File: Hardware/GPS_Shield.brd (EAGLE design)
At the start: 59.7 x 53.3 mm, 52 parts, among them J1 ARDUINO_R3_SHIELD, J2 USD_CONNECTOR, J3 DNP (GP-735-VERTICAL), U1 APK2112-3.3V, U2 GP3906-TLP, U3 TXB0108

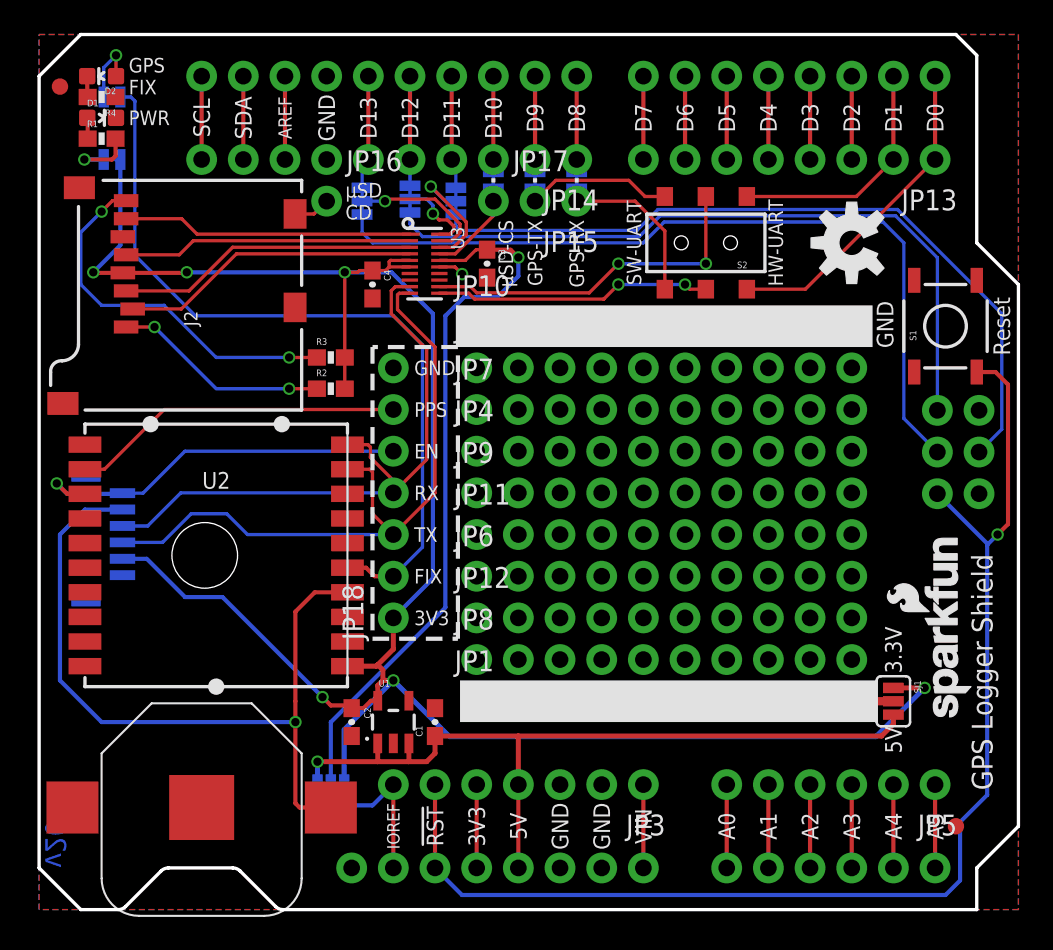
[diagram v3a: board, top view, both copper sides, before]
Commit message: Upping isolate to 0.01", adding some GND vias.
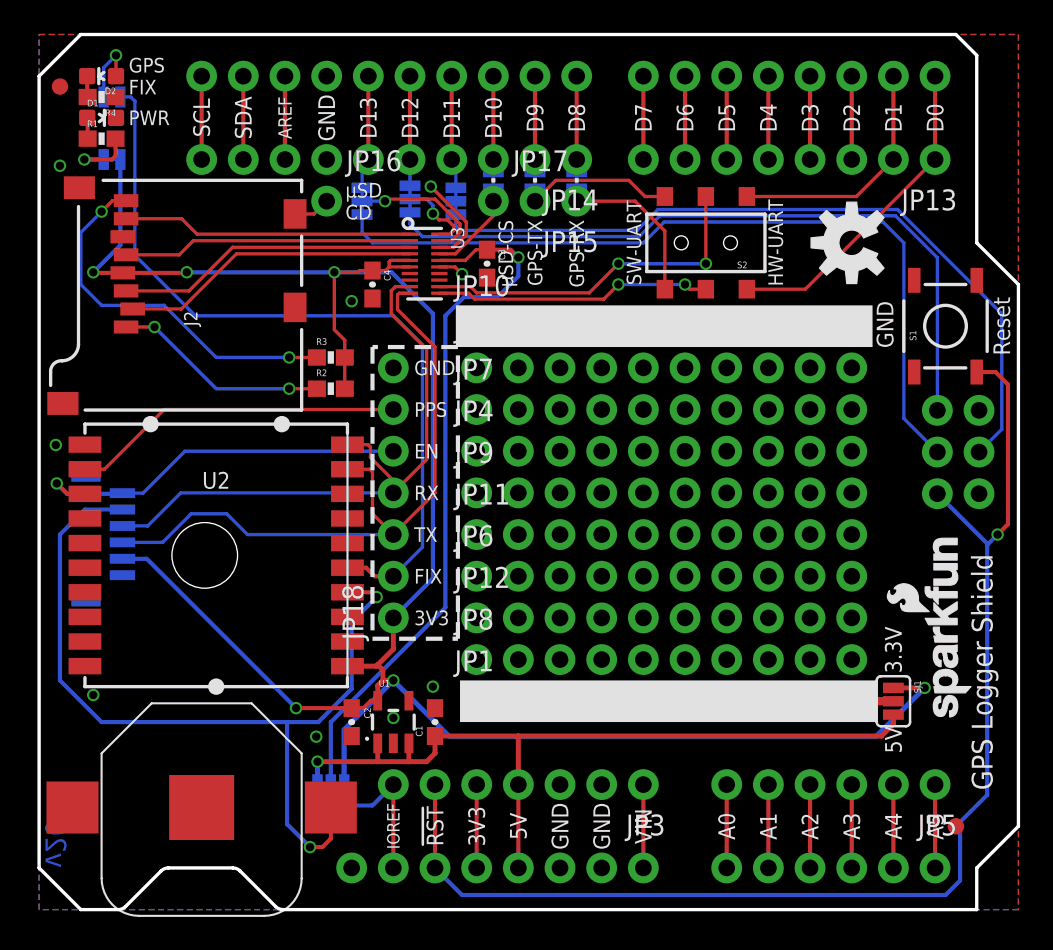
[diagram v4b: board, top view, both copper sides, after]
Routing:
- net V_BATT: track 46.3 -> 52.7 mm, vias 1 -> 2
- net 3.3V: track 134.0 -> 135.1 mm
- net GND: vias 1 -> 8
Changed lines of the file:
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@@
 <layer number="47" name="Measures" color="7" fill="1" visible="no" active="yes"/>
 <layer number="48" name="Document" color="7" fill="1" visible="no" active="yes"/>
-<layer number="49" name="Reference" color="7" fill="1" visible="yes" active="yes"/>
+<layer number="49" name="Reference" color="7" fill="1" visible="no" active="yes"/>
 <layer number="50" name="dxf" color="7" fill="1" visible="no" active="yes"/>
 <layer number="51" name="tDocu" color="6" fill="1" visible="yes" active="yes"/>
@@
 <contactref element="C4" pad="2"/>
 <contactref element="D1" pad="C"/>
-<polygon width="0.3048" layer="1" isolate="0.1524">
+<polygon width="0.254" layer="1" isolate="0.254">
 <vertex x="0" y="53.34"/>
 <vertex x="59.69" y="53.34"/>
@@
 <vertex x="0" y="0"/>
 </polygon>
-<polygon width="0.3048" layer="16" isolate="0.1524">
+<polygon width="0.254" layer="16" isolate="0.254">
 <vertex x="0" y="53.34"/>
 <vertex x="59.69" y="53.34"/>
@@
 <contactref element="J2" pad="GND3"/>
 <contactref element="J2" pad="GND"/>
+<via x="19.05" y="37.084" extent="1-16" drill="0.508"/>
+<via x="21.59" y="11.684" extent="1-16" drill="0.508"/>
+<via x="16.891" y="10.541" extent="1-16" drill="0.508"/>
+<via x="24.003" y="13.589" extent="1-16" drill="0.508"/>
+<via x="3.302" y="13.081" extent="1-16" drill="0.508"/>
+<via x="1.016" y="28.321" extent="1-16" drill="0.508"/>
+<via x="1.27" y="45.339" extent="1-16" drill="0.508"/>
 </signal>
 <signal name="3.3V">
@@
 <wire x1="22.595" y1="39.17" x2="21.336" y2="39.17" width="0.2032" layer="1"/>
 <via x="9.001575" y="38.846575" extent="1-16" drill="0.508"/>
-<wire x1="9.001575" y1="38.846575" x2="18.63" y2="38.846575" width="0.254" layer="16"/>
-<via x="18.63" y="38.846575" extent="1-16" drill="0.508"/>
+<wire x1="9.001575" y1="38.846575" x2="17.995" y2="38.846575" width="0.254" layer="16"/>
+<via x="17.995" y="38.846575" extent="1-16" drill="0.508"/>
 <wire x1="24.003" y1="36.322" x2="24.003" y2="20.193" width="0.254" layer="16"/>
 <wire x1="20.64" y1="12.7301" x2="20.2231" y2="12.7301" width="0.254" layer="1"/>
 <wire x1="20.2231" y1="12.7301" x2="19.773" y2="12.28" width="0.254" layer="1"/>
-<wire x1="19.05" y1="12.28" x2="19.773" y2="12.28" width="0.254" layer="1"/>
 <contactref element="JP18" pad="1"/>
 <wire x1="24.003" y1="20.193" x2="21.59" y2="17.78" width="0.254" layer="16"/>
-<wire x1="18.63" y1="38.846575" x2="21.478425" y2="38.846575" width="0.254" layer="16"/>
+<wire x1="17.995" y1="38.846575" x2="21.478425" y2="38.846575" width="0.254" layer="16"/>
 <wire x1="21.478425" y1="38.846575" x2="24.003" y2="36.322" width="0.254" layer="16"/>
 <wire x1="22.595" y1="39.57" x2="21.409" y2="39.57" width="0.2032" layer="1"/>
@@
 <wire x1="20.32" y1="38.95" x2="19.534425" y2="38.95" width="0.2032" layer="1"/>
 <wire x1="19.534425" y1="38.95" x2="19.431" y2="38.846575" width="0.2032" layer="1"/>
-<wire x1="18.63" y1="38.846575" x2="19.431" y2="38.846575" width="0.2032" layer="1"/>
+<wire x1="17.995" y1="38.846575" x2="19.431" y2="38.846575" width="0.2032" layer="1"/>
 <wire x1="21.336" y1="39.17" x2="21.116" y2="38.95" width="0.2032" layer="1"/>
 <wire x1="21.116" y1="38.95" x2="20.32" y2="38.95" width="0.2032" layer="1"/>
@@
 <wire x1="3.338575" y1="38.81" x2="3.302" y2="38.846575" width="0.254" layer="1"/>
 <wire x1="18.63" y1="31.75" x2="18.63" y2="33.655" width="0.2032" layer="1"/>
-<wire x1="18.63" y1="38.846575" x2="18.63" y2="33.655" width="0.2032" layer="1"/>
 <contactref element="J3" pad="2"/>
 <wire x1="5.08" y1="21.3835" x2="6.5565" y2="21.3835" width="0.254" layer="16"/>
-<via x="17.273" y="12.953" extent="1-16" drill="0.508"/>
-<wire x1="17.273" y1="12.953" x2="11.176" y2="19.05" width="0.254" layer="16"/>
-<wire x1="11.176" y1="19.05" x2="8.89" y2="19.05" width="0.254" layer="16"/>
-<wire x1="8.89" y1="19.05" x2="6.5565" y2="21.3835" width="0.254" layer="16"/>
-<wire x1="18.885" y1="12.445" x2="17.781" y2="12.445" width="0.254" layer="1"/>
-<wire x1="17.781" y1="12.445" x2="17.273" y2="12.953" width="0.254" layer="1"/>
+<wire x1="18.63" y1="33.655" x2="18.63" y2="34.71" width="0.2032" layer="1"/>
+<wire x1="17.995" y1="38.846575" x2="17.995" y2="35.345" width="0.2032" layer="1"/>
+<wire x1="17.995" y1="35.345" x2="18.63" y2="34.71" width="0.2032" layer="1"/>
+<wire x1="6.5565" y1="21.3835" x2="15.66" y2="12.28" width="0.254" layer="16"/>
+<via x="15.66" y="12.28" extent="1-16" drill="0.508"/>
+<wire x1="15.66" y1="12.28" x2="19.05" y2="12.28" width="0.254" layer="1"/>
+<wire x1="19.773" y1="12.28" x2="19.05" y2="12.28" width="0.254" layer="1"/>
 </signal>
 <signal name="5V">
@@
 <contactref element="J3" pad="5"/>
 <contactref element="U2" pad="4"/>
-<wire x1="15.621" y1="6.477" x2="15.621" y2="11.43" width="0.254" layer="1"/>
-<wire x1="15.621" y1="12.7" x2="15.621" y2="18.161" width="0.254" layer="1"/>
-<wire x1="18.795" y1="19.34" x2="16.8" y2="19.34" width="0.254" layer="1"/>
-<wire x1="16.8" y1="19.34" x2="15.621" y2="18.161" width="0.254" layer="1"/>
-<wire x1="15.621" y1="6.477" x2="15.875" y2="6.223" width="0.254" layer="1"/>
-<wire x1="17.78" y1="6.223" x2="15.875" y2="6.223" width="0.254" layer="1"/>
 <wire x1="5.08" y1="24.3835" x2="2.7935" y2="24.3835" width="0.254" layer="16"/>
 <wire x1="2.7935" y1="24.3835" x2="1.27" y2="22.86" width="0.254" layer="16"/>
 <wire x1="1.27" y1="22.86" x2="1.27" y2="13.97" width="0.254" layer="16"/>
 <wire x1="1.27" y1="13.97" x2="3.81" y2="11.43" width="0.254" layer="16"/>
-<wire x1="3.81" y1="11.43" x2="15.621" y2="11.43" width="0.254" layer="16"/>
-<via x="15.621" y="11.43" extent="1-16" drill="0.508"/>
-<wire x1="15.621" y1="11.43" x2="15.621" y2="12.7" width="0.254" layer="1"/>
+<wire x1="3.81" y1="11.43" x2="15.113" y2="11.43" width="0.254" layer="16"/>
+<wire x1="15.113" y1="11.43" x2="17.018" y2="11.43" width="0.254" layer="16"/>
+<wire x1="18.795" y1="19.34" x2="20.284" y2="19.34" width="0.254" layer="1"/>
+<wire x1="20.284" y1="19.34" x2="20.574" y2="19.05" width="0.254" layer="1"/>
+<via x="20.574" y="19.05" extent="1-16" drill="0.508"/>
+<wire x1="20.574" y1="19.05" x2="19.05" y2="17.526" width="0.254" layer="16"/>
+<wire x1="19.05" y1="17.526" x2="19.05" y2="13.462" width="0.254" layer="16"/>
+<wire x1="19.05" y1="13.462" x2="17.018" y2="11.43" width="0.254" layer="16"/>
+<wire x1="15.113" y1="11.43" x2="15.113" y2="5.207" width="0.254" layer="16"/>
+<wire x1="15.113" y1="5.207" x2="16.51" y2="3.81" width="0.254" layer="16"/>
+<via x="16.51" y="3.81" extent="1-16" drill="0.508"/>
+<wire x1="16.51" y1="3.81" x2="17.272" y2="3.81" width="0.254" layer="1"/>
+<wire x1="17.272" y1="3.81" x2="17.78" y2="4.318" width="0.254" layer="1"/>
+<wire x1="17.78" y1="4.318" x2="17.78" y2="6.223" width="0.254" layer="1"/>
 </signal>
 <signal name="CD">
